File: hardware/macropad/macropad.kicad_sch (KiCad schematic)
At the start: 27 parts, among them J1 SWD, J2 USB_C_Receptacle, J4 display(4x1), SW1 SW_Push, SW10 SW_SPDT, SW11 SW_Push, SW12 Enc1, SW13 Enc2, SW2 SW_Push, SW3 SW_Push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

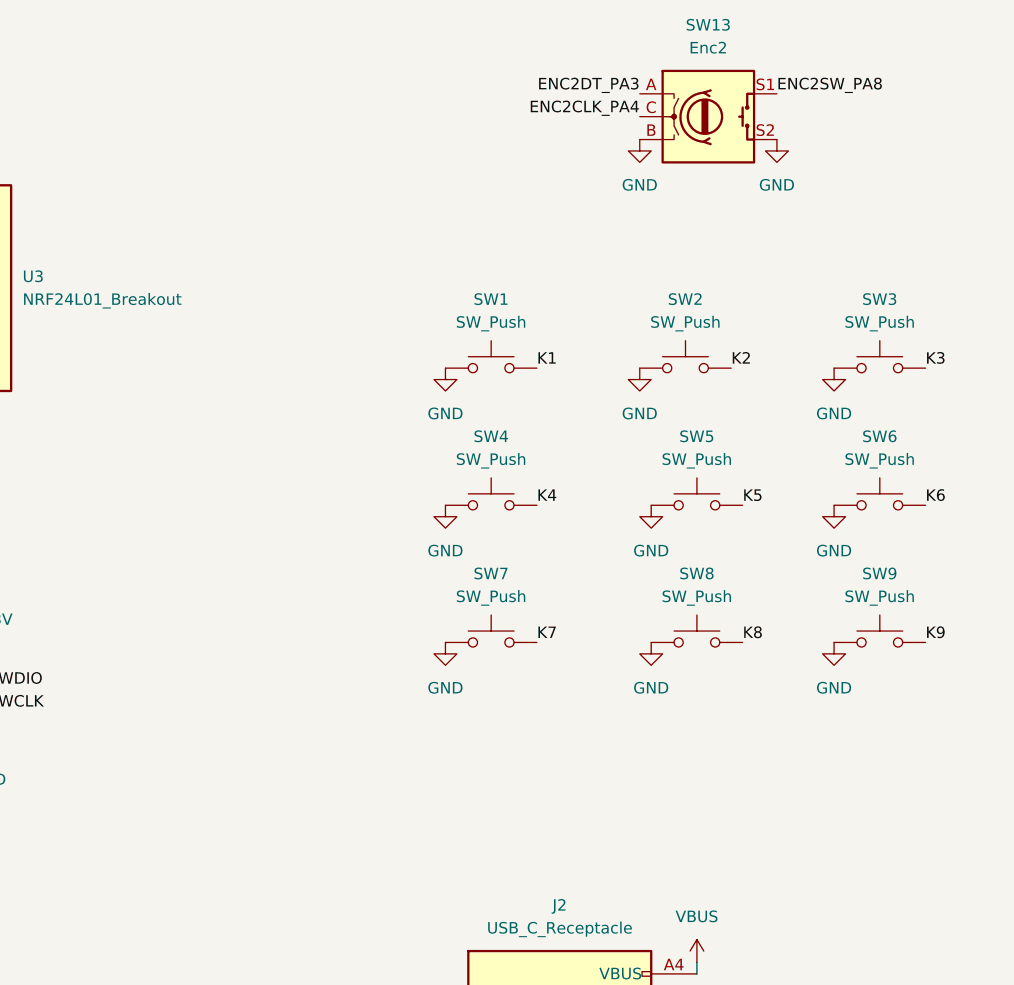
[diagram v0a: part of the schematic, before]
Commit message: added debouncing caps
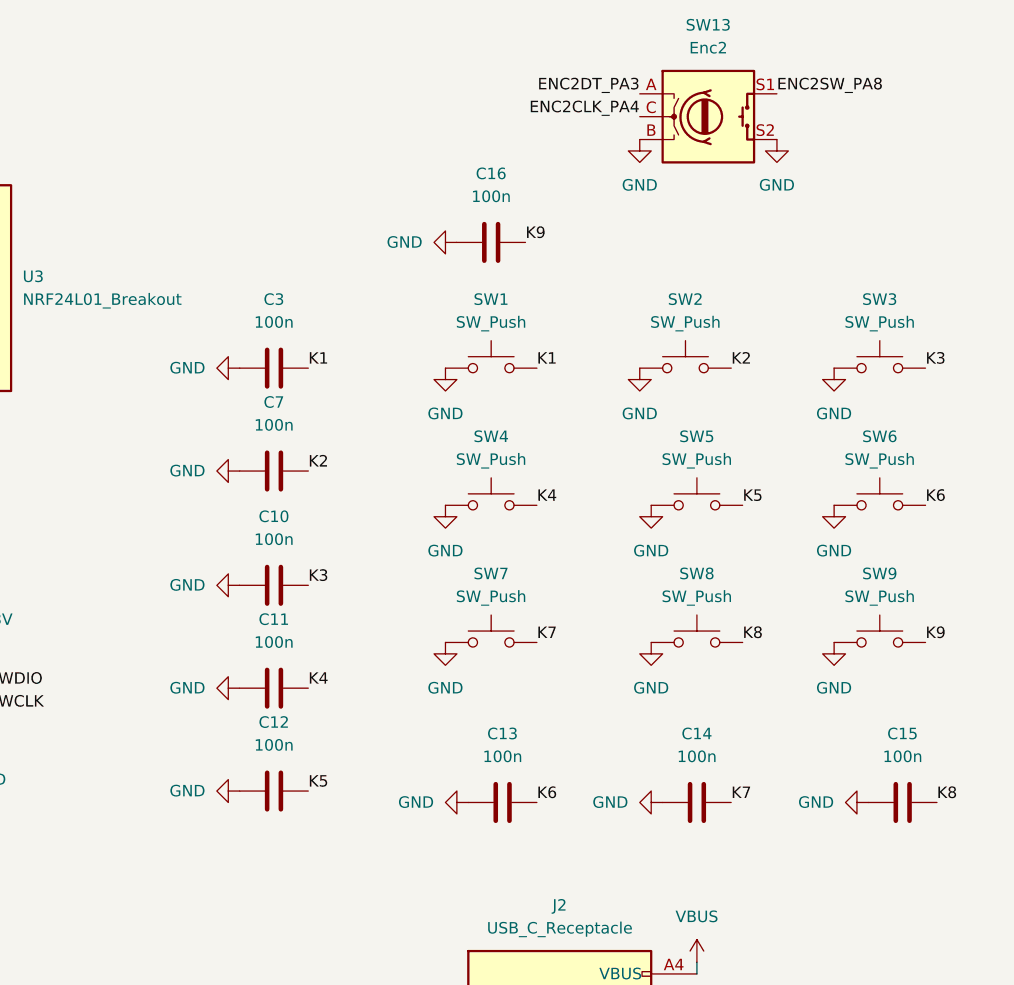
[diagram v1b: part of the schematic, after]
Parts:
- added C10, C11, C12, C13, C14, C15, C16, C3, C7: 100n, symbol Device:C
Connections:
- net GND: now also C10.1, C11.1, C12.1, C13.1, C14.1, C15.1, C16.1, C3.1, C7.1
- net K1: now also C3.2
- net K2: now also C7.2
- net K3: now also C10.2
- net K4: now also C11.2
- net K5: now also C12.2
- net K6: now also C13.2
- net K7: now also C14.2
- net K8: now also C15.2
- net K9: now also C16.2

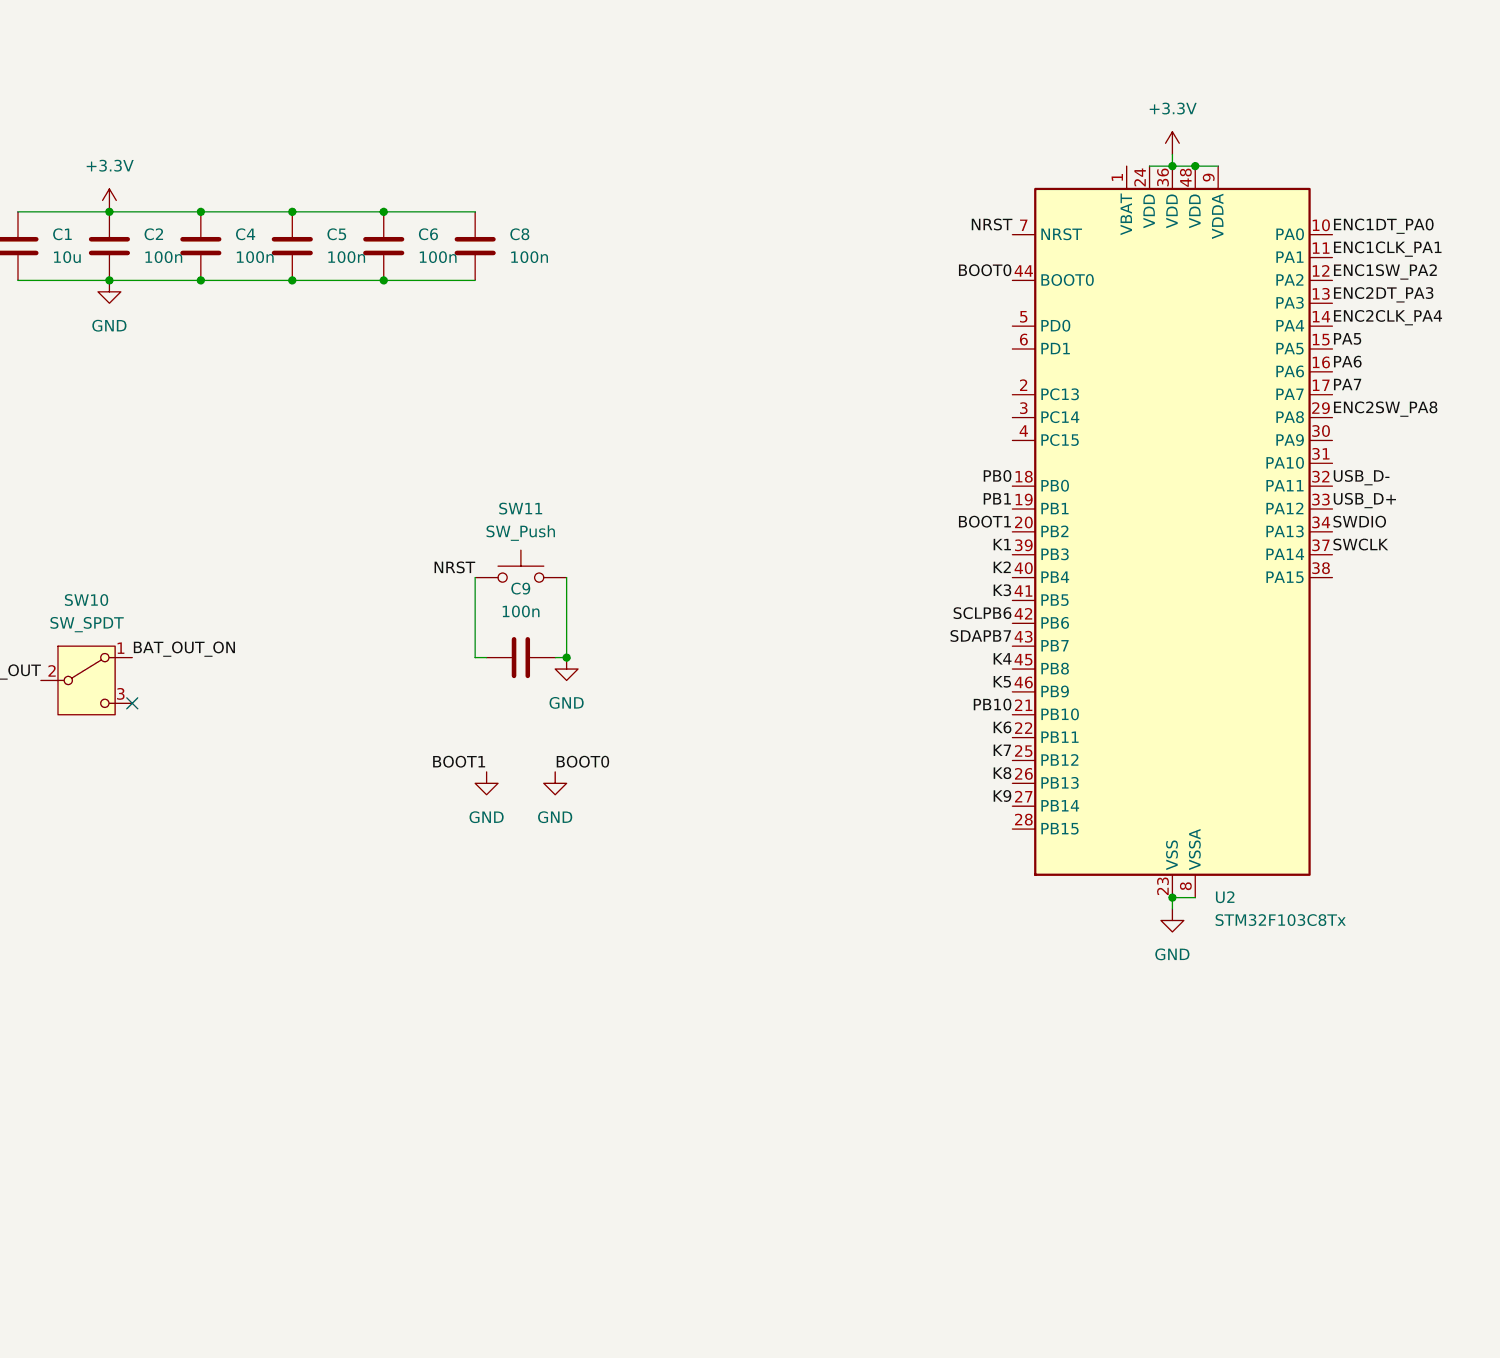
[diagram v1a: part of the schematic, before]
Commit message: changed load capacitance, added oscillator for pad
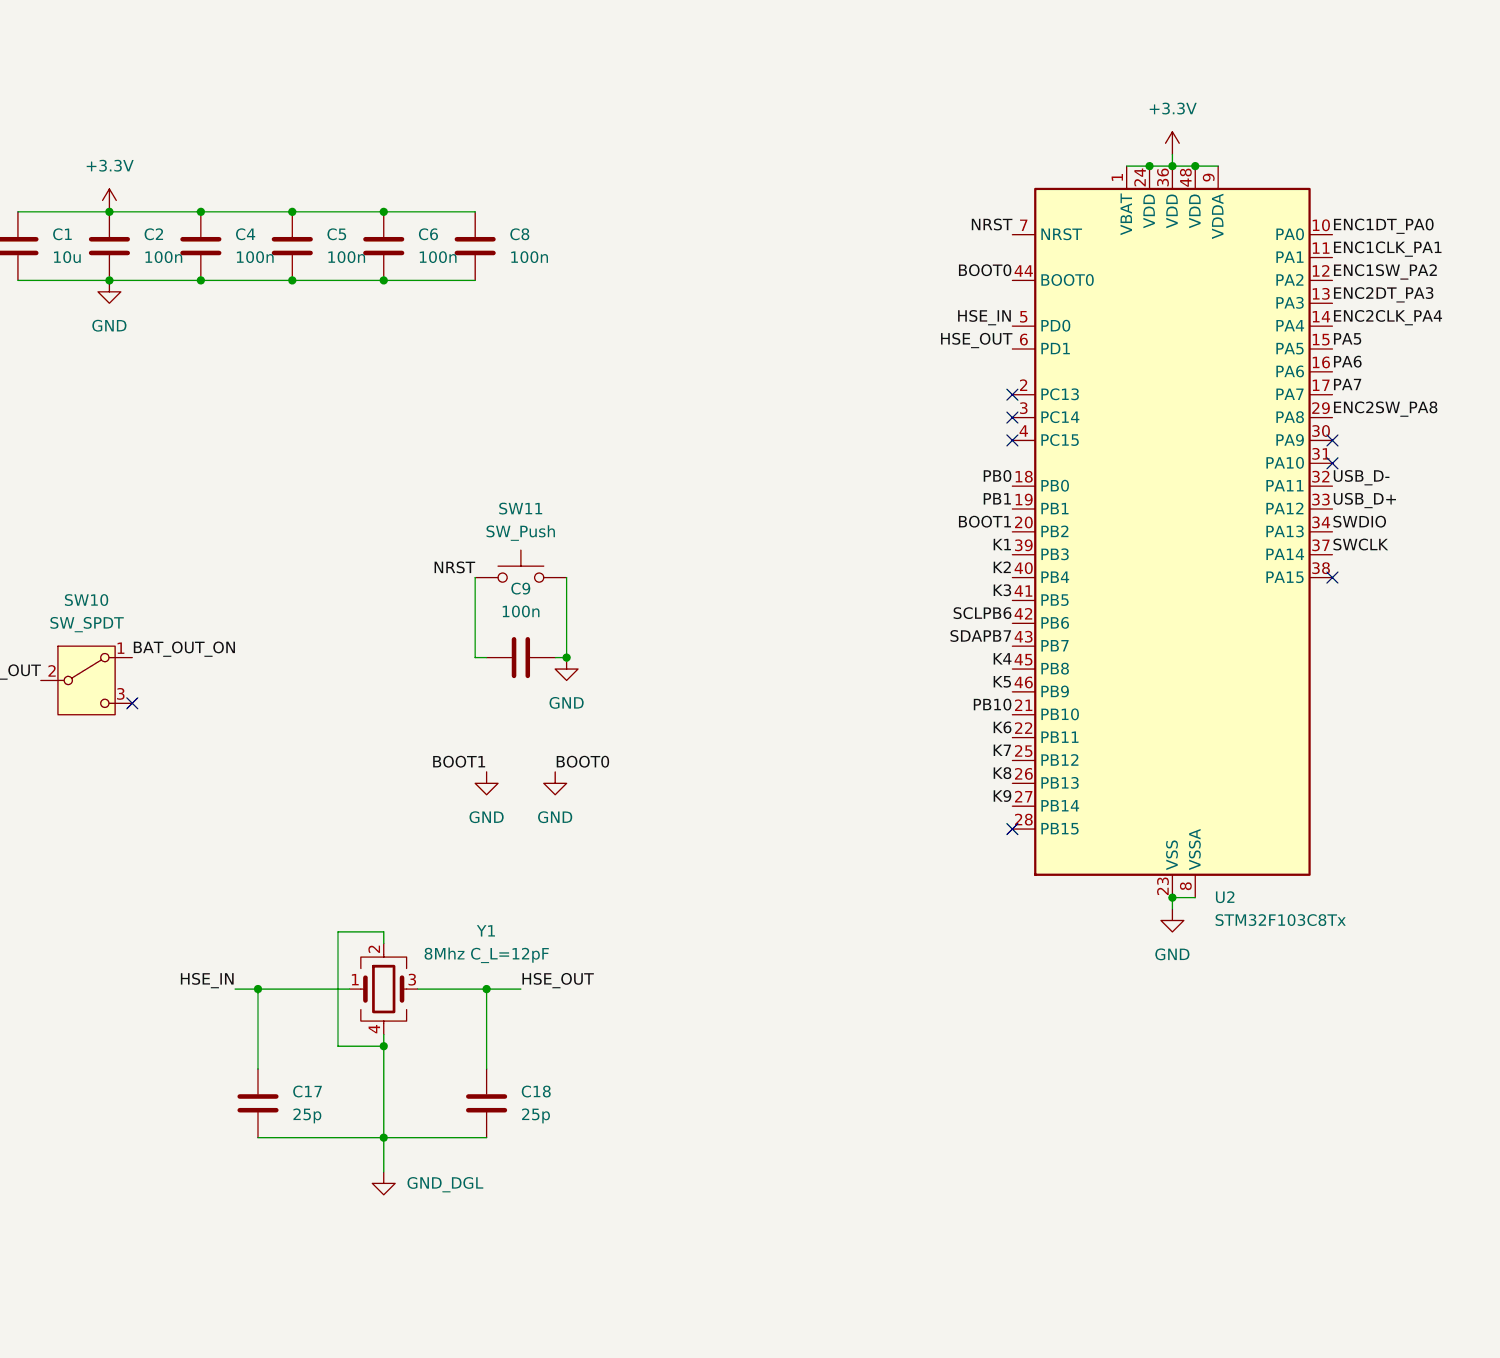
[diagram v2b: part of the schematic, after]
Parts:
- added C17, C18: 25p, Capacitor_SMD:C_0805_2012Metric, symbol Device:C
- added Y1: 8Mhz C_L=12pF, Crystal:Crystal_SMD_3225-4Pin_3.2x2.5mm, symbol Device:Crystal_GND24
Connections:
- net +3.3V: now also U2.1 (VBAT)
- net HSE_IN: now reaches U2.5 (PD0)
- net HSE_IN: now also C17.1, Y1.1
- net HSE_OUT: now reaches U2.6 (PD1)
- net HSE_OUT: now also C18.1, Y1.3
- new net GND_DGL: C17.2, C18.2, Y1.2, Y1.4
- no-connect marks 11 -> 18

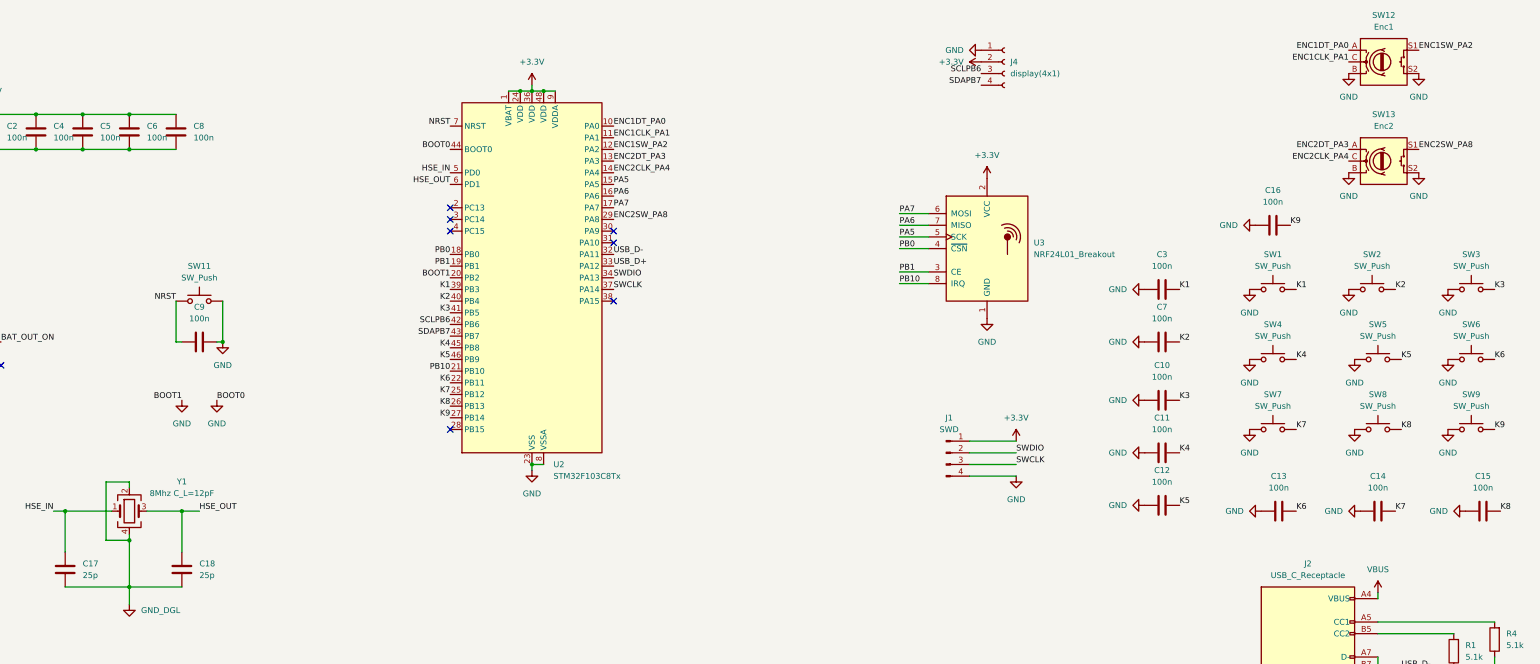
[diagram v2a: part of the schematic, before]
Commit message: update oscillator + passives'
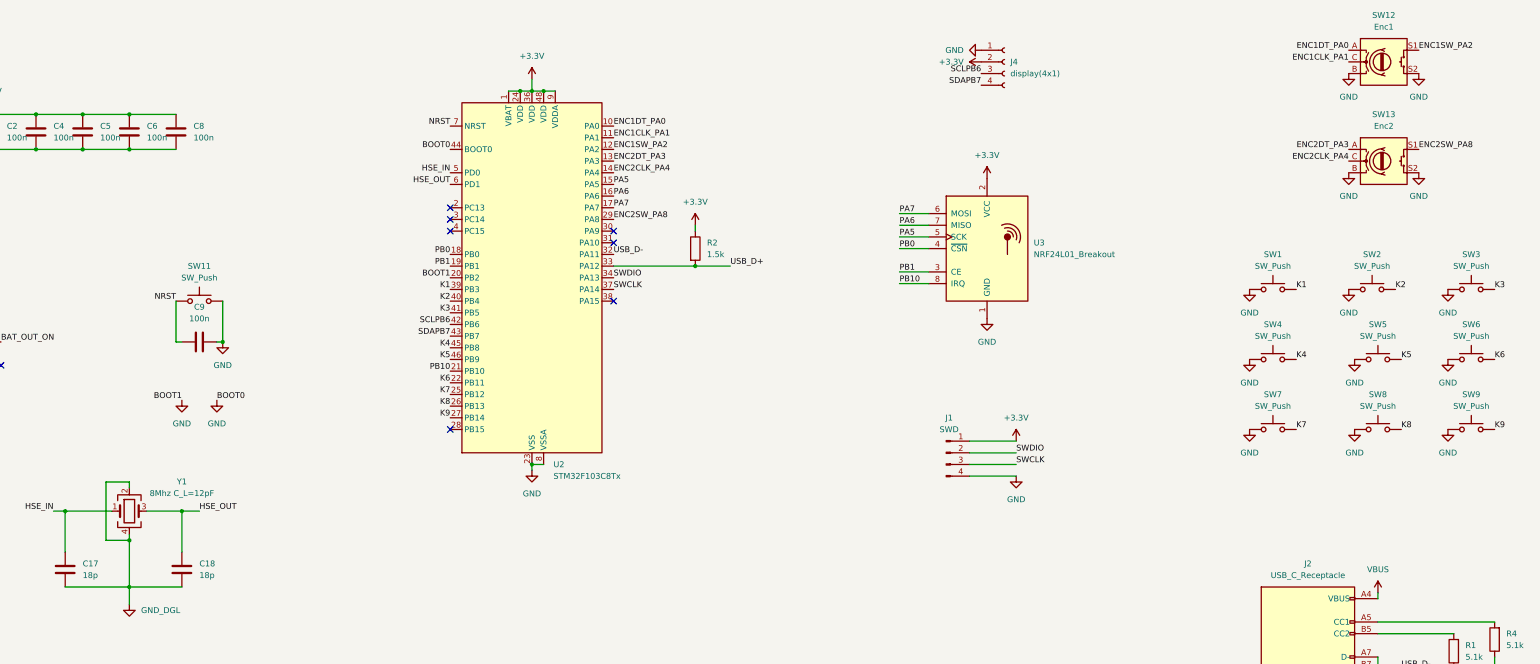
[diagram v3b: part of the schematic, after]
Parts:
- removed C10, C11, C12, C13, C14, C15, C16, C3, C7: 100n, symbol Device:C
- added R2: 1.5k, symbol Device:R
- C17, C18: value 25p -> 18p
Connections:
- net +3.3V: now also R2.1
- net USB_D+: now also R2.2

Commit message: something changed. i didnt track
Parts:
- added C3: 10u, symbol Device:C
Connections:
- net +3.3V: now also C3.1
- net GND: now also C3.2
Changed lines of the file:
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@@
 	)
 	(junction
+		(at 288.29 53.34)
+		(diameter 0)
+		(color 0 0 0 0)
+	)
+	(junction
+		(at 288.29 83.82)
+		(diameter 0)
+		(color 0 0 0 0)
+	)
+	(junction
 		(at 101.6 39.37)
 		(diameter 0)
@@
 	(wire
 		(pts
+			(xy 321.31 83.82) (xy 321.31 73.66)
+		)
+		(stroke
+			(width 0)
+			(type default)
+		)
+	)
+	(wire
+		(pts
 			(xy 87.63 125.73) (xy 97.79 125.73)
 		)
@@
 	(wire
 		(pts
+			(xy 288.29 49.53) (xy 288.29 53.34)
+		)
+		(stroke
+			(width 0)
+			(type default)
+		)
+	)
+	(wire
+		(pts
 			(xy 269.24 66.04) (xy 275.59 66.04)
 		)
@@
 	(wire
 		(pts
+			(xy 288.29 83.82) (xy 321.31 83.82)
+		)
+		(stroke
+			(width 0)
+			(type default)
+		)
+	)
+	(wire
+		(pts
 			(xy 87.63 142.24) (xy 101.6 142.24)
 		)
@@
 	(wire
 		(pts
+			(xy 321.31 66.04) (xy 321.31 53.34)
+		)
+		(stroke
+			(width 0)
+			(type default)
+		)
+	)
+	(wire
+		(pts
+			(xy 288.29 85.09) (xy 288.29 83.82)
+		)
+		(stroke
+			(width 0)
+			(type default)
+		)
+	)
+	(wire
+		(pts
 			(xy 85.09 125.73) (xy 87.63 125.73)
 		)
@@
 		)
 	)
+	(wire
+		(pts
+			(xy 321.31 53.34) (xy 288.29 53.34)
+		)
+		(stroke
+			(width 0)
+			(type default)
+		)
+	)
 	(label "PA7"
 		(at 269.24 60.96 0)
@@
 	(symbol
 		(lib_id "power:GND")
-		(at 288.29 83.82 0)
+		(at 288.29 85.09 0)
 		(unit 1)
 		(exclude_from_sim no)
@@
 		(fields_autoplaced yes)
 		(property "Reference" "#PWR021"
-			(at 288.29 90.17 0)
+			(at 288.29 91.44 0)
 			(effects
 				(font
@@
 		)
 		(property "Value" "GND"
-			(at 288.29 88.9 0)
+			(at 288.29 90.17 0)
 			(effects
 				(font
@@
 		)
 		(property "Footprint" ""
-			(at 288.29 83.82 0)
+			(at 288.29 85.09 0)
 			(effects
 				(font
@@
 		)
 		(property "Datasheet" ""
-			(at 288.29 83.82 0)
+			(at 288.29 85.09 0)
 			(effects
 				(font
@@
 		)
 		(property "Description" "Power symbol creates a global label with name \"GND\" , ground"
-			(at 288.29 83.82 0)
+			(at 288.29 85.09 0)
 			(effects
 				(font
@@
 	(symbol
 		(lib_id "power:+3.3V")
-		(at 288.29 53.34 0)
+		(at 288.29 49.53 0)
 		(unit 1)
 		(exclude_from_sim no)
@@
 		(fields_autoplaced yes)
 		(property "Reference" "#PWR020"
-			(at 288.29 57.15 0)
+			(at 288.29 53.34 0)
 			(effects
 				(font
@@
 		)
 		(property "Value" "+3.3V"
-			(at 288.29 48.26 0)
+			(at 288.29 44.45 0)
 			(effects
 				(font
@@
 		)
 		(property "Footprint" ""
-			(at 288.29 53.34 0)
+			(at 288.29 49.53 0)
 			(effects
 				(font
@@
 		)
 		(property "Datasheet" ""
-			(at 288.29 53.34 0)
+			(at 288.29 49.53 0)
 			(effects
 				(font
@@
 		)
 		(property "Description" "Power symbol creates a global label with name \"+3.3V\""
-			(at 288.29 53.34 0)
+			(at 288.29 49.53 0)
 			(effects
 				(font
@@
 					(unit 1)
 				)
+			)
+		)
+	)
+	(symbol
+		(lib_id "Device:C")
+		(at 321.31 69.85 0)
+		(unit 1)
+		(exclude_from_sim no)
+		(in_bom yes)
+		(on_board yes)
+		(dnp no)
+		(fields_autoplaced yes)
+		(property "Reference" "C3"
+			(at 325.12 68.5799 0)
+			(effects
+				(font
+					(size 1.27 1.27)
+				)
+				(justify left)
+			)
+		)
+		(property "Value" "10u"
+			(at 325.12 71.1199 0)
+			(effects
+				(font
+					(size 1.27 1.27)
+				)
+				(justify left)
+			)
+		)
+		(property "Footprint" ""
+			(at 322.2752 73.66 0)
+			(effects
+				(font
+					(size 1.27 1.27)
+				)
+				(hide yes)
+			)
+		)
+		(property "Datasheet" "~"
+			(at 321.31 69.85 0)
+			(effects
+				(font
+					(size 1.27 1.27)
+				)
+				(hide yes)
+			)
+		)
+		(property "Description" "Unpolarized capacitor"
+			(at 321.31 69.85 0)
+			(effects
+				(font
+					(size 1.27 1.27)
+				)
+				(hide yes)
+			)
+		)
+		(pin "2"
+		)
+		(pin "1"
+		)
+		(instances
+			(project "macropad"
+				(path "/228dc472-b306-4e5f-8dc5-2bf23eb4978d"
+					(reference "C3")
+					(unit 1)
+				)
